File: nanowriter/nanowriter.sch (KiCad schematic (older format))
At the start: 19 parts, among them IC1 ATMEGA32U2, J1 USB_mini_micro_B, K1 KEYSW, K2 KEYSW, K3 KEYSW, K4 KEYSW, K5 KEYSW, K6 KEYSW, SW1 SW_PUSH, X1 XTAL_GND

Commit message: Rev 1 pcb
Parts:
- removed C1, C2: 22p, Capacitors_SMD:C_0805_HandSoldering, symbol C
- removed C3: 0.1u, Capacitors_SMD:C_0805_HandSoldering, symbol C
- removed C4: 4.7u, Capacitors_SMD:C_0805_HandSoldering, symbol C
- removed C5: 1u, Capacitors_SMD:C_0805_HandSoldering, symbol C
- removed IC1: ATMEGA32U2, keyboard_parts:QFP32, symbol ATMEGA32U2
- removed J1: USB_mini_micro_B, keyboard_parts:USB_microB, symbol USB_mini_micro_B
- removed R1, R2: 10k, Resistors_SMD:R_0805_HandSoldering, symbol R
- removed R3, R4: 22, Resistors_SMD:R_0805_HandSoldering, symbol R
- removed SW1: SW_PUSH, Buttons_Switches_SMD:SW_SPST_TL3342, symbol SW_PUSH
- removed X1: XTAL_GND, keyboard_parts:FA-238, symbol XTAL_GND
- added U1: ProMicro, keebs:Pro_Micro, symbol ProMicro
- K1, K2, K3, K4, K5, K6: footprint keebs:Mx_Alps_100 -> Keyboard:CHERRY_PCB_100H
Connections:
- net labels removed: VCC
- wire segments 66 -> 29

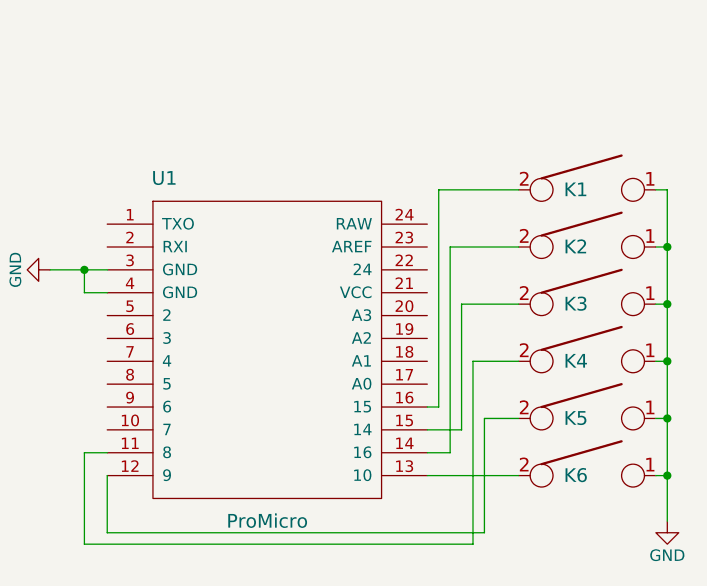
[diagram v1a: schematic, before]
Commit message: Rev. 2 board
- Minimized dimension
- Added mounting holes
- Added reset switch with pullup
- Fixed pins 13-24 on pro-micro being backwards
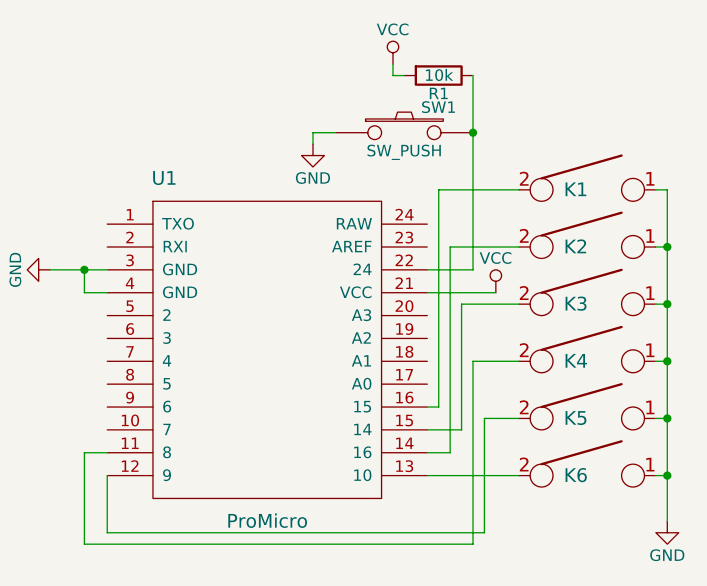
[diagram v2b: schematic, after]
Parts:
- added R1: 10k, Resistors_SMD:R_0805_HandSoldering, symbol R
- added SW1: SW_PUSH, Buttons_Switches_SMD:SW_SPST_TL3342, symbol SW_PUSH
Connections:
- net GND: now also SW1.1
- net VCC: now reaches U1.21 (VCC)
- net VCC: now also R1.2
- net at U1.22 (24): now also R1.1, SW1.2
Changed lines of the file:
@@
 Connection ~ 7650 4350
 Connection ~ 7650 4600
-$Comp
-L ProMicro U1
-U 1 1 58880220
-P 5900 4250
-F 0 "U1" H 5450 5200 60  0000 C CNN
-F 1 "ProMicro" H 5900 3700 60  0000 C CNN
-F 2 "keebs:Pro_Micro" H 6000 3200 60  0001 C CNN
-F 3 "" H 6000 3200 60  0000 C CNN
-	1    5900 4250
-	1    0    0    -1
-$EndComp
 Wire Wire Line
 	6600 4300 6650 4300
@@
 	6850 4350 7000 4350
 Wire Wire Line
-	6600 4600 7000 4600
-Wire Wire Line
 	4950 3700 5200 3700
 Wire Wire Line
@@
 $EndComp
 Connection ~ 5100 3700
+$Comp
+L ProMicro U1
+U 1 1 58A091D4
+P 5900 4250
+F 0 "U1" H 5450 5200 60  0000 C CNN
+F 1 "ProMicro" H 5900 3700 60  0000 C CNN
+F 2 "keebs:Pro_Micro" H 6000 3200 60  0001 C CNN
+F 3 "" H 6000 3200 60  0000 C CNN
+	1    5900 4250
+	1    0    0    -1
+$EndComp
+Wire Wire Line
+	7000 4600 6600 4600
+$Comp
+L SW_PUSH SW1
+U 1 1 58A0941F
+P 6500 3100
+F 0 "SW1" H 6650 3210 50  0000 C CNN
+F 1 "SW_PUSH" H 6500 3020 50  0000 C CNN
+F 2 "Buttons_Switches_SMD:SW_SPST_TL3342" H 6500 3100 60  0001 C CNN
+F 3 "" H 6500 3100 60  0000 C CNN
+	1    6500 3100
+	1    0    0    -1
+$EndComp
+Wire Wire Line
+	6800 3700 6600 3700
+$Comp
+L GND #PWR03
+U 1 1 58A094DC
+P 6100 3150
+F 0 "#PWR03" H 6100 2900 50  0001 C CNN
+F 1 "GND" H 6100 3000 50  0000 C CNN
+F 2 "" H 6100 3150 50  0000 C CNN
+F 3 "" H 6100 3150 50  0000 C CNN
+	1    6100 3150
+	1    0    0    -1
+$EndComp
+Wire Wire Line
+	6200 3100 6100 3100
+Wire Wire Line
+	6100 3100 6100 3150
+$Comp
+L R R1
+U 1 1 58A0952F
+P 6650 2850
+F 0 "R1" V 6730 2850 50  0000 C CNN
+F 1 "10k" V 6650 2850 50  0000 C CNN
+F 2 "Resistors_SMD:R_0805_HandSoldering" V 6580 2850 50  0001 C CNN
+F 3 "" H 6650 2850 50  0000 C CNN
+	1    6650 2850
+	0    1    1    0
+$EndComp
+Connection ~ 6800 3100
+$Comp
+L VCC #PWR?
+U 1 1 58A0989C
+P 6900 3800
+F 0 "#PWR?" H 6900 3650 50  0001 C CNN
+F 1 "VCC" H 6900 3950 50  0000 C CNN
+F 2 "" H 6900 3800 50  0000 C CNN
+F 3 "" H 6900 3800 50  0000 C CNN
+	1    6900 3800
+	1    0    0    -1
+$EndComp
+Wire Wire Line
+	6800 2850 6800 3700
+$Comp
+L VCC #PWR?
+U 1 1 58A09F90
+P 6450 2800
+F 0 "#PWR?" H 6450 2650 50  0001 C CNN
+F 1 "VCC" H 6450 2950 50  0000 C CNN
+F 2 "" H 6450 2800 50  0000 C CNN
+F 3 "" H 6450 2800 50  0000 C CNN
+	1    6450 2800
+	1    0    0    -1
+$EndComp
+Wire Wire Line
+	6450 2800 6450 2850
+Wire Wire Line
+	6450 2850 6500 2850
+Wire Wire Line
+	6600 3800 6900 3800
 $EndSCHEMATC

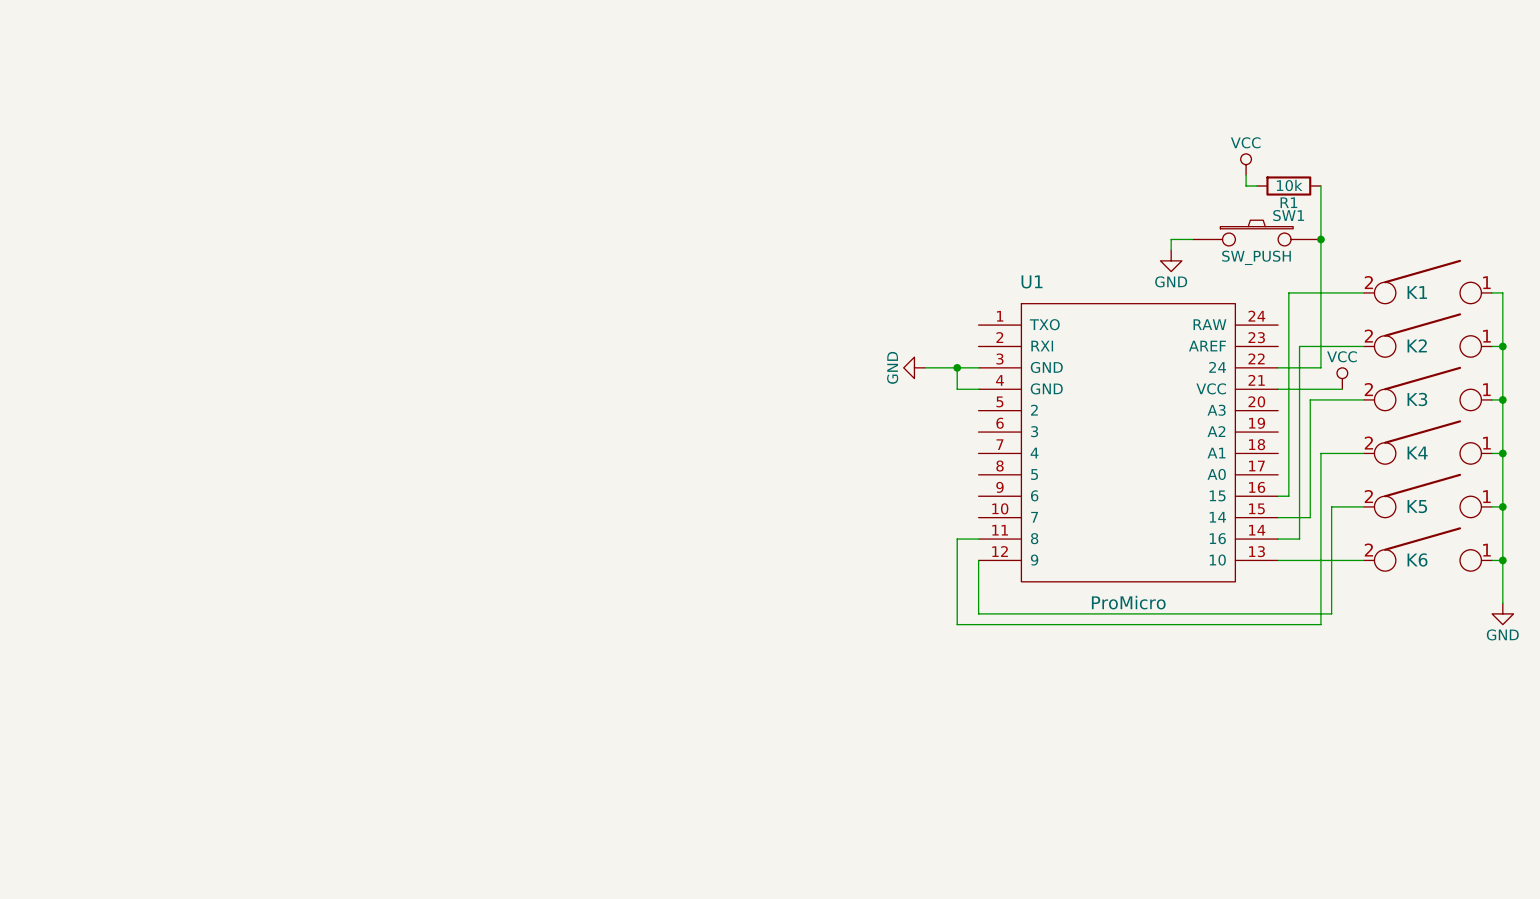
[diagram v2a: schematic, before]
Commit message: PCB rev 3. Changed from Pro Micro based design to directly using an Atmega32u2
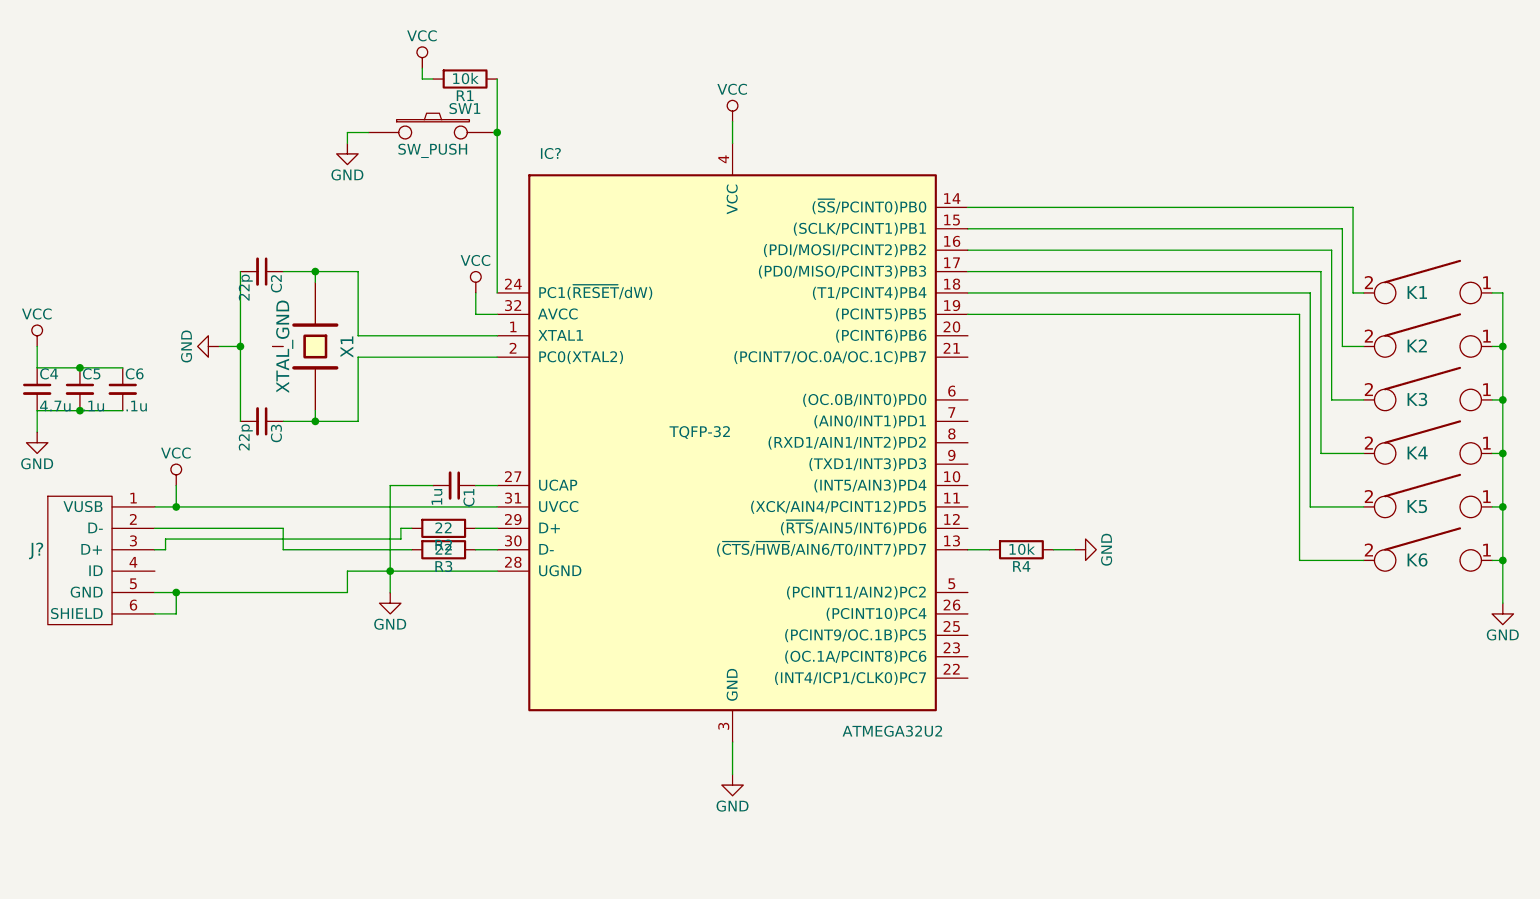
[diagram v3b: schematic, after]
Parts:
- removed U1: ProMicro, keebs:Pro_Micro, symbol ProMicro
- added C1: 1u, symbol C_Small
- added C2, C3: 22p, symbol C_Small
- added C4: 4.7u, symbol C_Small
- added C5, C6: .1u, symbol C_Small
- added IC?: ATMEGA32U2, TQFP-32, symbol ATMEGA32U2
- added J?: USB_mini_micro_B, symbol USB_mini_micro_B
- added R2, R3: 22, symbol R
- added R4: 10k, symbol R
- added X1: XTAL_GND, symbol XTAL_GND
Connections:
- net GND: now also C1.2, C2.2, C3.2, C4.2, C5.2, C6.2, IC?.28 (UGND), IC?.3 (GND), J?.5 (GND), J?.6 (SHIELD), R4.1
- net VCC: now also C4.1, C5.1, C6.1, IC?.31 (UVCC), IC?.32 (AVCC), IC?.4 (VCC), J?.1 (VUSB)
- net at K1.2: now also IC?.14 ((~SS~/PCINT0)PB0)
- net at K2.2: now also IC?.15 ((SCLK/PCINT1)PB1)
- net at K3.2: now also IC?.16 ((PDI/MOSI/PCINT2)PB2)
- net at K4.2: now also IC?.17 ((PD0/MISO/PCINT3)PB3)
- net at K5.2: now also IC?.18 ((T1/PCINT4)PB4)
- net at K6.2: now also IC?.19 ((PCINT5)PB5)
- net at R1.1, SW1.2: now also IC?.24 (PC1(~RESET~/dW))
- new net: C2.1, IC?.1 (XTAL1), X1.1
- new net: IC?.13 ((~CTS~/~HWB~/AIN6/T0/INT7)PD7), R4.2
- new net: C3.1, IC?.2 (PC0(XTAL2)), X1.2
- new net: C1.1, IC?.27 (UCAP)
- new net: IC?.29 (D+), R2.1
- new net: IC?.30 (D-), R3.1
- new net: J?.2 (D-), R3.2
- new net: J?.3 (D+), R2.2
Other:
- moved on the sheet: R1, SW1

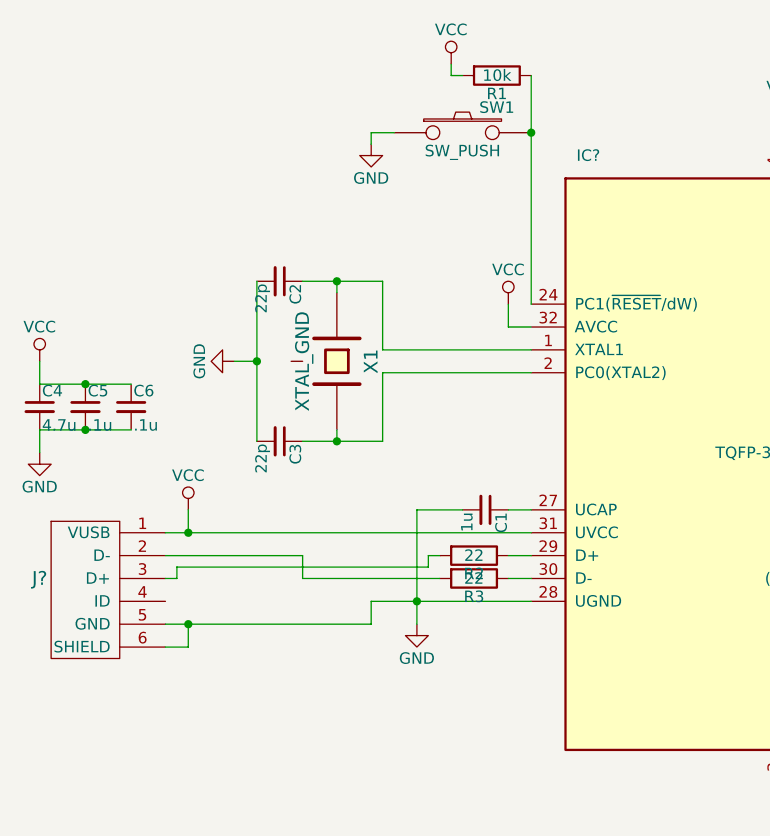
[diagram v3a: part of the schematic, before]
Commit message: PCB rev 4. Changed to all smd usb port.
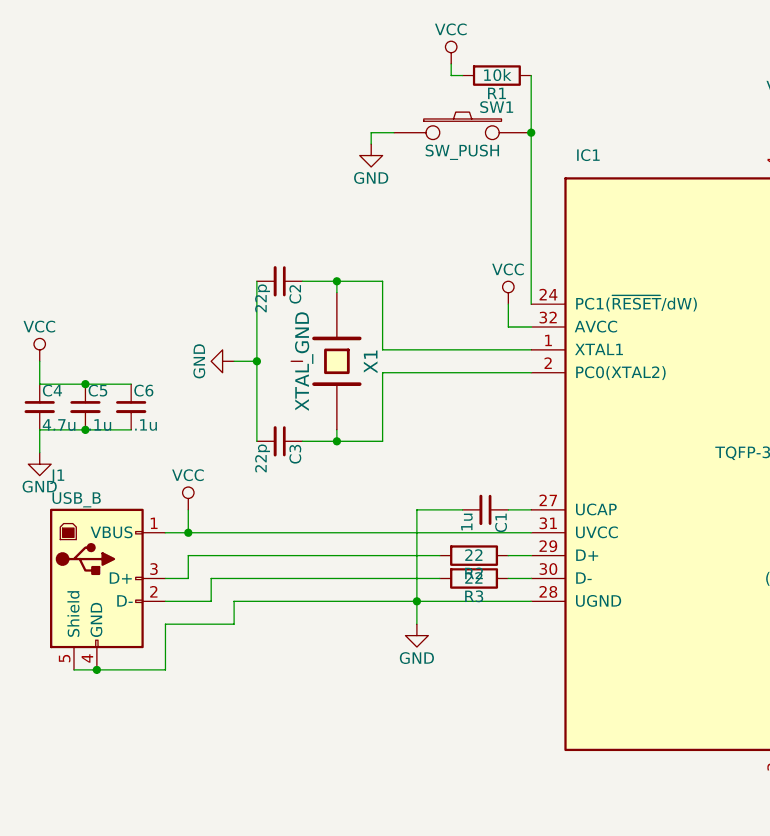
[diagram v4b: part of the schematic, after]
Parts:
- removed J?: USB_mini_micro_B, symbol USB_mini_micro_B
- added J1: USB_B, Connectors_Molex:USB_Micro-B_Molex_47346-0001, symbol USB_B
- C1, C2, C3, C4, C5, C6: footprint (none) -> Capacitors_SMD:C_0805_HandSoldering
- K1, K2, K3, K4, K5, K6: footprint Keyboard:CHERRY_PCB_100H -> TheKeebrary:MX_PCB_100H
- R2, R3, R4: footprint (none) -> Resistors_SMD:R_0805_HandSoldering
- X1: footprint (none) -> Crystals:Crystal_SMD_Abracon_ABM8G-4pin_3.2x2.5mm
- gave numbers to parts that had none: 1
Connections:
- net GND: now also J1.4 (GND), J1.5 (Shield)
- net VCC: now also J1.1 (VBUS)
- net at R3.2: now also J1.2 (D-)
- net at R2.2: now also J1.3 (D+)
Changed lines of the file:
@@
 LIBS:contrib
 LIBS:valves
-LIBS:keyboard_parts
-LIBS:teensy
 LIBS:nanowriter-cache
 EELAYER 25 0
@@
 F 0 "K1" H 7250 3350 60  0000 C CNN
 F 1 "KEYSW" H 7300 3250 60  0001 C CNN
-F 2 "Keyboard:CHERRY_PCB_100H" H 7300 3350 60  0001 C CNN
+F 2 "TheKeebrary:MX_PCB_100H" H 7300 3350 60  0001 C CNN
 F 3 "" H 7300 3350 60  0000 C CNN
 	1    7300 3350
@@
 F 0 "K2" H 7250 3600 60  0000 C CNN
 F 1 "KEYSW" H 7300 3500 60  0001 C CNN
-F 2 "Keyboard:CHERRY_PCB_100H" H 7300 3600 60  0001 C CNN
+F 2 "TheKeebrary:MX_PCB_100H" H 7300 3600 60  0001 C CNN
 F 3 "" H 7300 3600 60  0000 C CNN
 	1    7300 3600
@@
 F 0 "K3" H 7250 3850 60  0000 C CNN
 F 1 "KEYSW" H 7300 3750 60  0001 C CNN
-F 2 "Keyboard:CHERRY_PCB_100H" H 7300 3850 60  0001 C CNN
+F 2 "TheKeebrary:MX_PCB_100H" H 7300 3850 60  0001 C CNN
 F 3 "" H 7300 3850 60  0000 C CNN
 	1    7300 3850
@@
 F 0 "K4" H 7250 4100 60  0000 C CNN
 F 1 "KEYSW" H 7300 4000 60  0001 C CNN
-F 2 "Keyboard:CHERRY_PCB_100H" H 7300 4100 60  0001 C CNN
+F 2 "TheKeebrary:MX_PCB_100H" H 7300 4100 60  0001 C CNN
 F 3 "" H 7300 4100 60  0000 C CNN
 	1    7300 4100
@@
 F 0 "K5" H 7250 4350 60  0000 C CNN
 F 1 "KEYSW" H 7300 4250 60  0001 C CNN
-F 2 "Keyboard:CHERRY_PCB_100H" H 7300 4350 60  0001 C CNN
+F 2 "TheKeebrary:MX_PCB_100H" H 7300 4350 60  0001 C CNN
 F 3 "" H 7300 4350 60  0000 C CNN
 	1    7300 4350
@@
 F 0 "K6" H 7250 4600 60  0000 C CNN
 F 1 "KEYSW" H 7300 4500 60  0001 C CNN
-F 2 "Keyboard:CHERRY_PCB_100H" H 7300 4600 60  0001 C CNN
+F 2 "TheKeebrary:MX_PCB_100H" H 7300 4600 60  0001 C CNN
 F 3 "" H 7300 4600 60  0000 C CNN
 	1    7300 4600
@@
 $EndComp
 $Comp
-L ATMEGA32U2 IC?
+L ATMEGA32U2 IC1
 U 1 1 58C5F98C
 P 4050 4050
-F 0 "IC?" H 3200 5400 50  0000 C CNN
+F 0 "IC1" H 3200 5400 50  0000 C CNN
 F 1 "ATMEGA32U2" H 4800 2700 50  0000 C CNN
 F 2 "TQFP-32" H 3900 4100 50  0000 C CNN
@@
 F 0 "X1" H 2100 3750 60  0000 C CNN
 F 1 "XTAL_GND" H 2100 3450 60  0000 C CNN
-F 2 "" H 2100 3600 60  0000 C CNN
+F 2 "Crystals:Crystal_SMD_Abracon_ABM8G-4pin_3.2x2.5mm" H 2100 3600 60  0001 C CNN
 F 3 "" H 2100 3600 60  0000 C CNN
 	1    2100 3600
@@
 F 0 "C2" H 1860 3320 50  0000 L CNN
 F 1 "22p" H 1860 3170 50  0000 L CNN
-F 2 "" H 1850 3250 50  0000 C CNN
+F 2 "Capacitors_SMD:C_0805_HandSoldering" H 1850 3250 50  0001 C CNN
 F 3 "" H 1850 3250 50  0000 C CNN
 	1    1850 3250
@@
 F 0 "C3" H 1860 4020 50  0000 L CNN
 F 1 "22p" H 1860 3870 50  0000 L CNN
-F 2 "" H 1850 3950 50  0000 C CNN
+F 2 "Capacitors_SMD:C_0805_HandSoldering" H 1850 3950 50  0001 C CNN
 F 3 "" H 1850 3950 50  0000 C CNN
 	1    1850 3950
@@
 F 0 "R4" V 5480 4550 50  0000 C CNN
 F 1 "10k" V 5400 4550 50  0000 C CNN
-F 2 "" V 5330 4550 50  0000 C CNN
+F 2 "Resistors_SMD:R_0805_HandSoldering" V 5330 4550 50  0001 C CNN
 F 3 "" H 5400 4550 50  0000 C CNN
 	1    5400 4550
@@
 $EndComp
 $Comp
-L USB_mini_micro_B J?
-U 1 1 58C61AEB
-P 1200 4500
-F 0 "J?" H 800 4450 60  0000 C CNN
-F 1 "USB_mini_micro_B" H 1050 4750 60  0001 C CNN
-F 2 "" H 1150 4500 60  0000 C CNN
-F 3 "" H 1150 4500 60  0000 C CNN
-	1    1200 4500
-	1    0    0    -1
-$EndComp
-$Comp
 L R R2
 U 1 1 58C61C5E
@@
 F 0 "R2" V 2780 4450 50  0000 C CNN
 F 1 "22" V 2700 4450 50  0000 C CNN
-F 2 "" V 2630 4450 50  0000 C CNN
+F 2 "Resistors_SMD:R_0805_HandSoldering" V 2630 4450 50  0001 C CNN
 F 3 "" H 2700 4450 50  0000 C CNN
 	1    2700 4450
@@
 F 0 "R3" V 2780 4550 50  0000 C CNN
 F 1 "22" V 2700 4550 50  0000 C CNN
-F 2 "" V 2630 4550 50  0000 C CNN
+F 2 "Resistors_SMD:R_0805_HandSoldering" V 2630 4550 50  0001 C CNN
 F 3 "" H 2700 4550 50  0000 C CNN
 	1    2700 4550
@@
 F 0 "C1" H 2760 4320 50  0000 L CNN
 F 1 "1u" H 2760 4170 50  0000 L CNN
-F 2 "" H 2750 4250 50  0000 C CNN
+F 2 "Capacitors_SMD:C_0805_HandSoldering" H 2750 4250 50  0001 C CNN
 F 3 "" H 2750 4250 50  0000 C CNN
 	1    2750 4250
@@
 	2950 4550 2850 4550
 Wire Wire Line
-	1950 4550 2550 4550
-Wire Wire Line
-	1950 4550 1950 4450
-Wire Wire Line
-	1950 4450 1350 4450
-Wire Wire Line
-	1350 4550 1400 4550
-Wire Wire Line
-	1400 4550 1400 4500
-Wire Wire Line
-	1400 4500 2500 4500
-Wire Wire Line
-	2500 4500 2500 4450
-Wire Wire Line
-	2500 4450 2550 4450
+	1550 4550 2550 4550
+Wire Wire Line
+	1450 4450 2550 4450
 Wire Wire Line
 	2950 4250 2850 4250
@@
 	2450 4250 2450 4750
 Wire Wire Line
-	2250 4650 2950 4650
+	1650 4650 2950 4650
 Connection ~ 2450 4650
-Wire Wire Line
-	1350 4750 2250 4750
-Wire Wire Line
-	2250 4750 2250 4650
-Wire Wire Line
-	1350 4850 1450 4850
-Wire Wire Line
-	1450 4850 1450 4750
-Connection ~ 1450 4750
 Wire Wire Line
 	7000 3350 6950 3350
@@
 F 0 "C4" H 810 3870 50  0000 L CNN
 F 1 "4.7u" H 810 3720 50  0000 L CNN
-F 2 "" H 800 3800 50  0000 C CNN
+F 2 "Capacitors_SMD:C_0805_HandSoldering" H 800 3800 50  0001 C CNN
 F 3 "" H 800 3800 50  0000 C CNN
 	1    800  3800
@@
 F 0 "C5" H 1010 3870 50  0000 L CNN
 F 1 ".1u" H 1010 3720 50  0000 L CNN
-F 2 "" H 1000 3800 50  0000 C CNN
+F 2 "Capacitors_SMD:C_0805_HandSoldering" H 1000 3800 50  0001 C CNN
 F 3 "" H 1000 3800 50  0000 C CNN
 	1    1000 3800
@@
 F 0 "C6" H 1210 3870 50  0000 L CNN
 F 1 ".1u" H 1210 3720 50  0000 L CNN
-F 2 "" H 1200 3800 50  0000 C CNN
+F 2 "Capacitors_SMD:C_0805_HandSoldering" H 1200 3800 50  0001 C CNN
 F 3 "" H 1200 3800 50  0000 C CNN
 	1    1200 3800
@@
 	800  3900 1200 3900
 Connection ~ 1000 3900
+$Comp
+L USB_B J1
+U 1 1 5946E4C1
+P 1050 4550
+F 0 "J1" H 850 5000 50  0000 L CNN
+F 1 "USB_B" H 850 4900 50  0000 L CNN
+F 2 "Connectors_Molex:USB_Micro-B_Molex_47346-0001" H 1200 4500 50  0001 C CNN
+F 3 "" H 1200 4500 50  0001 C CNN
+	1    1050 4550
+	1    0    0    -1
+$EndComp
+Wire Wire Line
+	1450 4450 1450 4550
+Wire Wire Line
+	1450 4550 1350 4550
+Wire Wire Line
+	1350 4650 1550 4650
+Wire Wire Line
+	1550 4650 1550 4550
+Wire Wire Line
+	950  4950 1350 4950
+Wire Wire Line
+	1350 4950 1350 4750
+Wire Wire Line
+	1350 4750 1650 4750
+Wire Wire Line
+	1650 4750 1650 4650
+Connection ~ 1050 4950
 $EndSCHEMATC
